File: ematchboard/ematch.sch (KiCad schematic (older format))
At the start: 28 parts

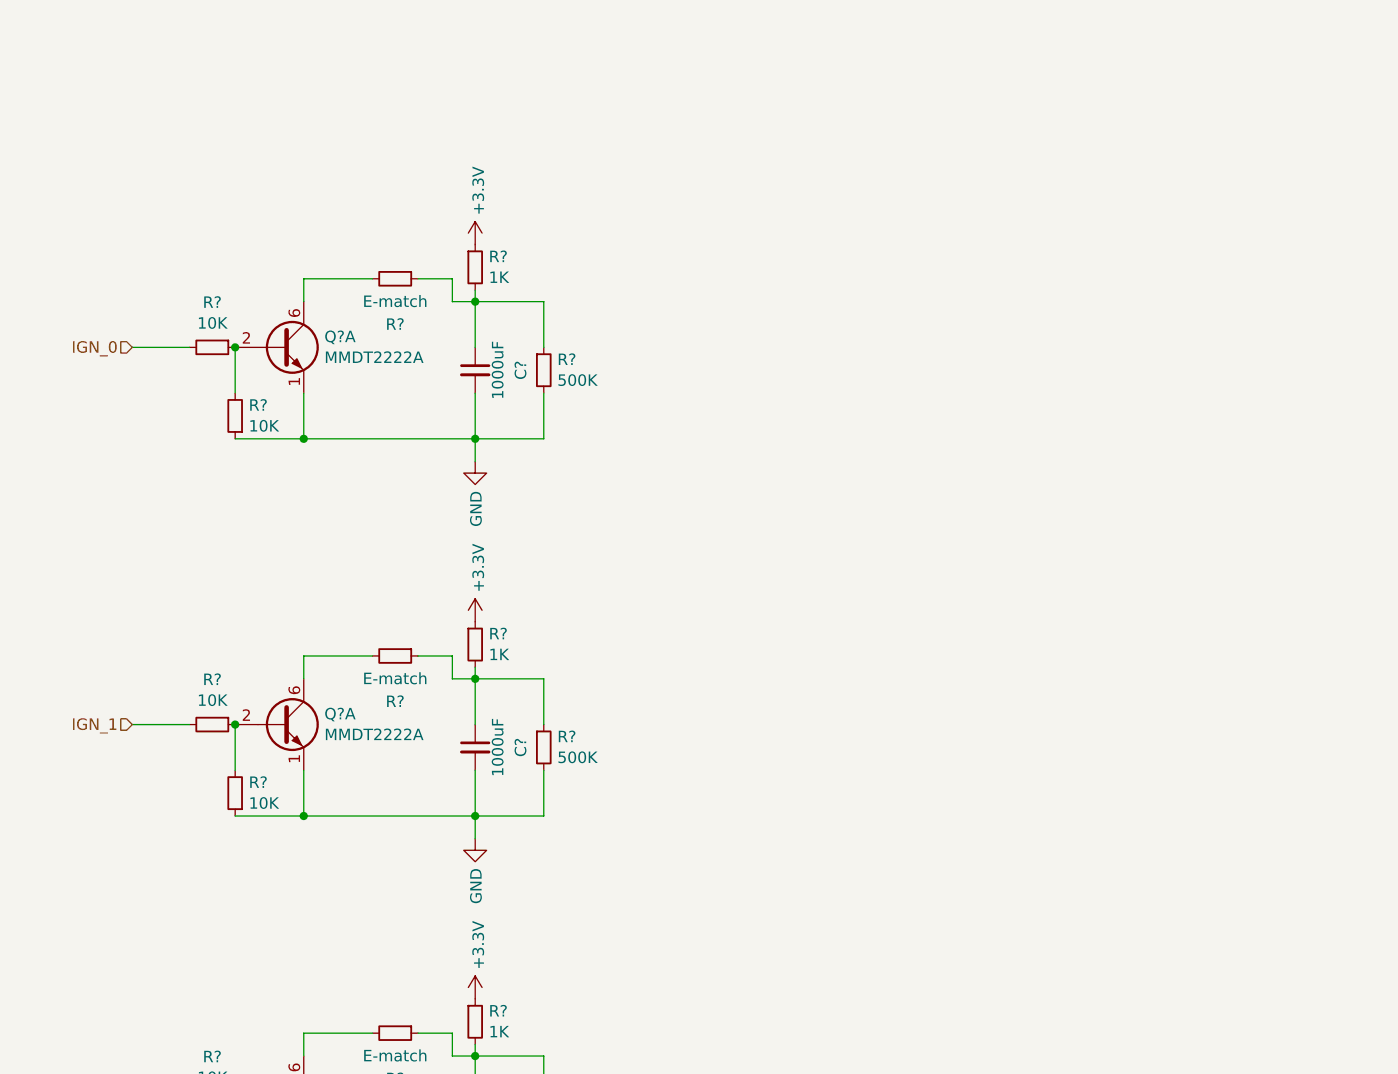
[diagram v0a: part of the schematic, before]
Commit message: Updated number of ematches
Increased e match count from 4->6 as requested (2 spares)
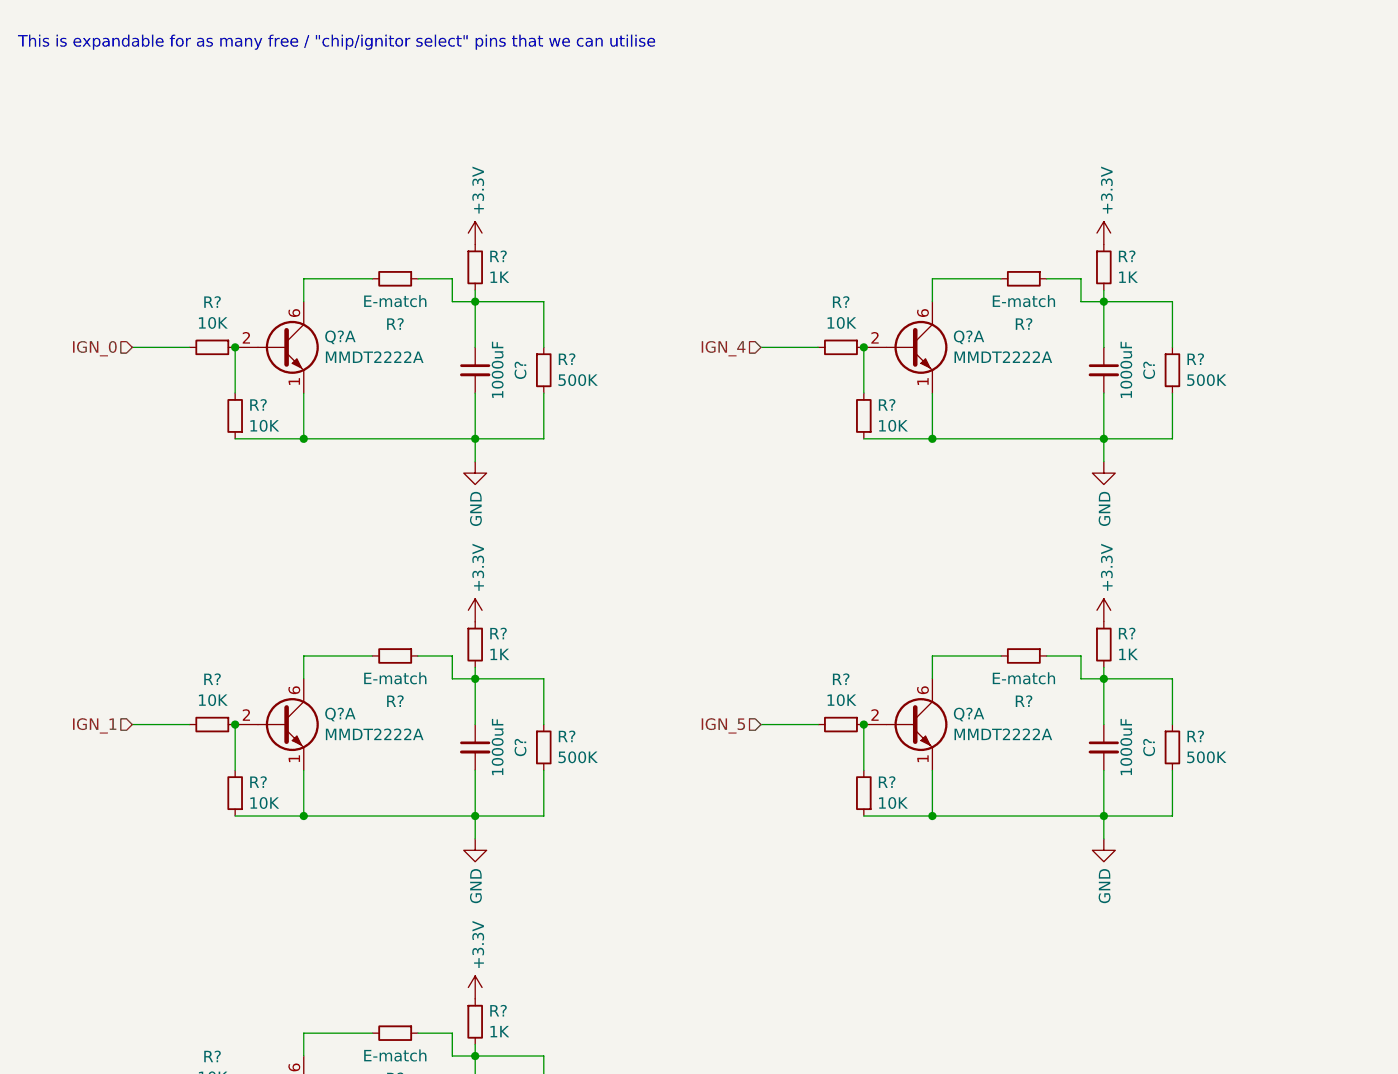
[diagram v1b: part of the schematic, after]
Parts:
- added C? (x2): 1000uF, symbol Device:C_Small
- added Q? (x2): MMDT2222A, Package_TO_SOT_SMD:SOT-363_SC-70-6, symbol Transistor_BJT:MMDT2222A
- added R? (x4): 10K, symbol Device:R_Small
- added R? (x2): 500K, symbol Device:R_Small
- added R? (x2): E-match, symbol Device:R_Small
- added R? (x2): 1K, symbol Device:R_Small
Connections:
- net +3V3: now also R?.1, R?.1
- net GND: now also C?.2, C?.2, Q?.1 (E1), Q?.1 (E1), R?.1, R?.1, R?.2, R?.2
- new net: Q?.2 (B1), R?.1, R?.2 (x2)
- new net: Q?.6 (C1), R?.2 (x2)
- new net: C?.1, R?.1, R?.1, R?.2 (x2)
- new net IGN_4: R?.2
- new net IGN_5: R?.2
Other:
- note added: "This is expandable for as many free / "chip/ignitor select" pins that we can utilise"
